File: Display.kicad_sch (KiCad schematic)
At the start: 9 parts, among them J2 TFT_LCD, U3 MT9284

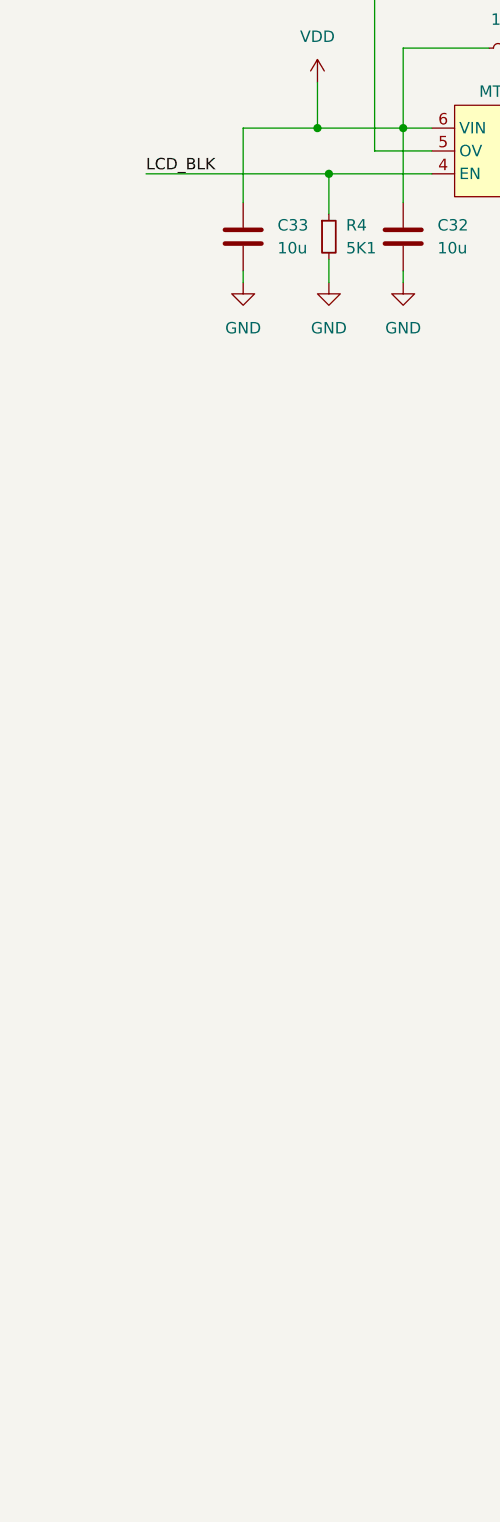
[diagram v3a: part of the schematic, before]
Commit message: Looks like FPC should be changed to XF2M-4015-1A
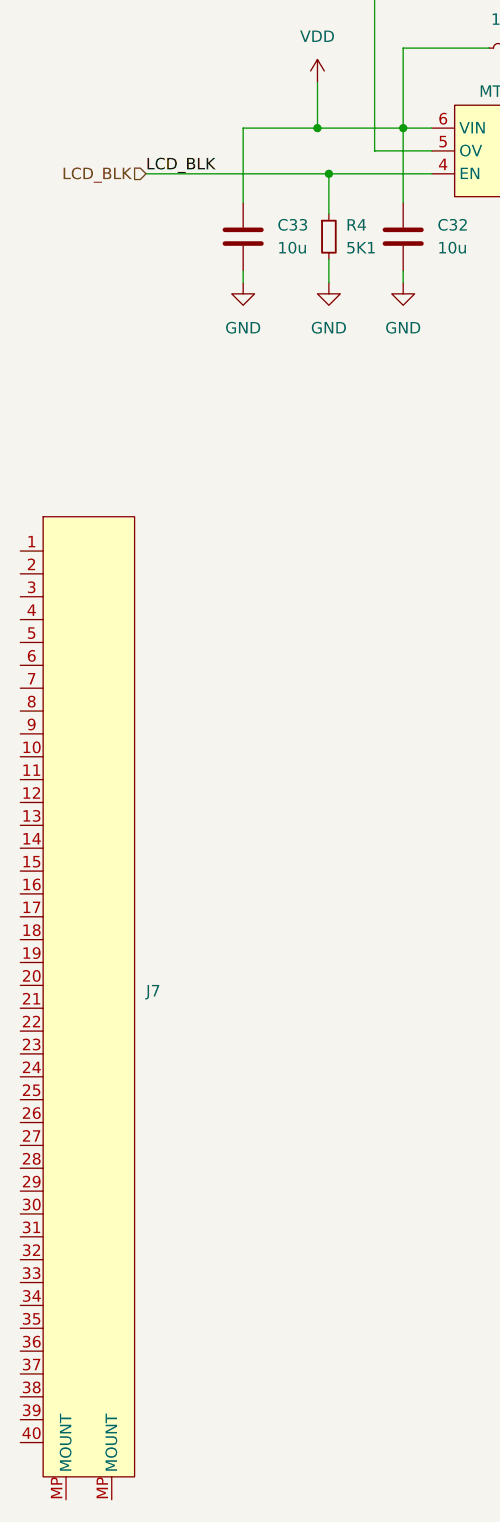
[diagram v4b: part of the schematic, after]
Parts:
- added J7: ~, FPC-40P-Omron-XF2M-4015-1Apretty:Omron-XF2M-4015-1A-R100-0-0-0, symbol FPC_40P_double_contact:FPC-40P
- D1: JLCPCB Part # (none) -> C345958
- J2: JLCPCB Part # (none) -> C225713
- R4: JLCPCB Part # (none) -> C25905
- U3: JLCPCB Part # (none) -> C181780
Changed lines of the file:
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@@
+		)
+	)
+	(hierarchical_label "LCD_BLK"
+		(shape input)
+		(at 57.15 48.26 180)
+		(fields_autoplaced yes)
+		(effects
+			(font
+				(size 1.27 1.27)
+			)
+			(justify right)
 		)
 	)
@@
 			)
 		)
+		(property "JLCPCB Part #" "C25905"
+			(at 77.47 55.245 0)
+			(effects
+				(font
+					(size 1.27 1.27)
+				)
+				(hide yes)
+			)
+		)
 		(pin "1"
 		)
@@
 			)
 		)
+		(property "JLCPCB Part #" ""
+			(at 97.79 34.29 0)
+			(effects
+				(font
+					(size 1.27 1.27)
+				)
+				(hide yes)
+			)
+		)
 		(pin "1"
 		)
@@
 			)
 		)
+		(property "JLCPCB Part #" ""
+			(at 67.945 55.245 0)
+			(effects
+				(font
+					(size 1.27 1.27)
+				)
+				(hide yes)
+			)
+		)
 		(pin "1"
 		)
@@
 			)
 		)
+		(property "JLCPCB Part #" ""
+			(at 113.03 53.34 0)
+			(effects
+				(font
+					(size 1.27 1.27)
+				)
+				(hide yes)
+			)
+		)
 		(pin "1"
 		)
@@
 			)
 		)
+		(property "JLCPCB Part #" ""
+			(at 85.725 55.245 0)
+			(effects
+				(font
+					(size 1.27 1.27)
+				)
+				(hide yes)
+			)
+		)
 		(pin "1"
 		)
@@
 		)
 		(property "Description" ""
+			(at 123.19 53.34 0)
+			(effects
+				(font
+					(size 1.27 1.27)
+				)
+				(hide yes)
+			)
+		)
+		(property "JLCPCB Part #" ""
 			(at 123.19 53.34 0)
 			(effects
@@
 			)
 		)
+		(property "JLCPCB Part #" "C345958"
+			(at 116.84 43.18 0)
+			(effects
+				(font
+					(size 1.27 1.27)
+				)
+				(hide yes)
+			)
+		)
 		(pin "1"
 		)
@@
 			)
 		)
+		(property "JLCPCB Part #" "C225713"
+			(at 209.55 133.35 0)
+			(effects
+				(font
+					(size 1.27 1.27)
+				)
+				(hide yes)
+			)
+		)
 		(pin "1"
 		)
@@
 			)
 		)
+		(property "JLCPCB Part #" "C181780"
+			(at 104.14 40.64 0)
+			(effects
+				(font
+					(size 1.27 1.27)
+				)
+				(hide yes)
+			)
+		)
 		(pin "1"
 		)
@@
 					(unit 1)
 				)
+			)
+		)
+	)
+	(symbol
+		(lib_name "FPC-40P_1")
+		(lib_id "FPC_40P_double_contact:FPC-40P")
+		(at 45.72 86.36 0)
+		(unit 1)
+		(exclude_from_sim no)
+		(in_bom yes)
+		(on_board yes)
+		(dnp no)
+		(fields_autoplaced yes)
+		(property "Reference" "J7"
+			(at 57.15 139.0649 0)
+			(effects
+				(font
+					(size 1.27 1.27)
+				)
+				(justify left)
+			)
+		)
+		(property "Value" "~"
+			(at 57.15 140.97 0)
+			(effects
+				(font
+					(size 1.27 1.27)
+				)
+				(justify left)
+			)
+		)
+		(property "Footprint" "FPC-40P-Omron-XF2M-4015-1Apretty:Omron-XF2M-4015-1A-R100-0-0-0"
+			(at 45.72 86.36 0)
+			(effects
+				(font
+					(size 1.27 1.27)
+				)
+				(hide yes)
+			)
+		)
+		(property "Datasheet" ""
+			(at 45.72 86.36 0)
+			(effects
+				(font
+					(size 1.27 1.27)
+				)
+				(hide yes)
+			)
+		)
+		(property "Description" ""
+			(at 45.72 86.36 0)
+			(effects
+				(font
+					(size 1.27 1.27)
+				)
+				(hide yes)
+			)
+		)
+		(pin "33"
+		)
+		(pin "17"
+		)
+		(pin "30"
+		)
+		(pin "32"
+		)
+		(pin "38"
+		)
+		(pin "2"
+		)
+		(pin "40"
+		)
+		(pin "34"
+		)
+		(pin "31"
+		)
+		(pin "27"
+		)
+		(pin "5"
+		)
+		(pin "4"
+		)
+		(pin "22"
+		)
+		(pin "6"
+		)
+		(pin "25"
+		)
+		(pin "9"
+		)
+		(pin "20"
+		)
+		(pin "36"
+		)
+		(pin "37"
+		)
+		(pin "12"
+		)
+		(pin "11"
+		)
+		(pin "10"
+		)
+		(pin "1"
+		)
+		(pin "8"
+		)
+		(pin "13"
+		)
+		(pin "MP"
+		)
+		(pin "14"
+		)
+		(pin "16"
+		)
+		(pin "21"
+		)
+		(pin "26"
+		)
+		(pin "19"
+		)
+		(pin "15"
+		)
+		(pin "39"
+		)
+		(pin "29"
+		)
+		(pin "35"
+		)
+		(pin "23"
+		)
+		(pin "24"
+		)
+		(pin "3"
+		)
+		(pin "7"
+		)
+		(pin "28"
+		)
+		(pin "18"
+		)
+		(pin "MP"
+		)
+		(instances
+			(project "H743_LCD_dev"
+				(path "/70094798-b7e4-48a4-a512-b8f48be18f9f/99abf84f-89dd-4209-b43f-cdbcbe391aaa"
+					(reference "J7")
+					(unit 1)
+				)

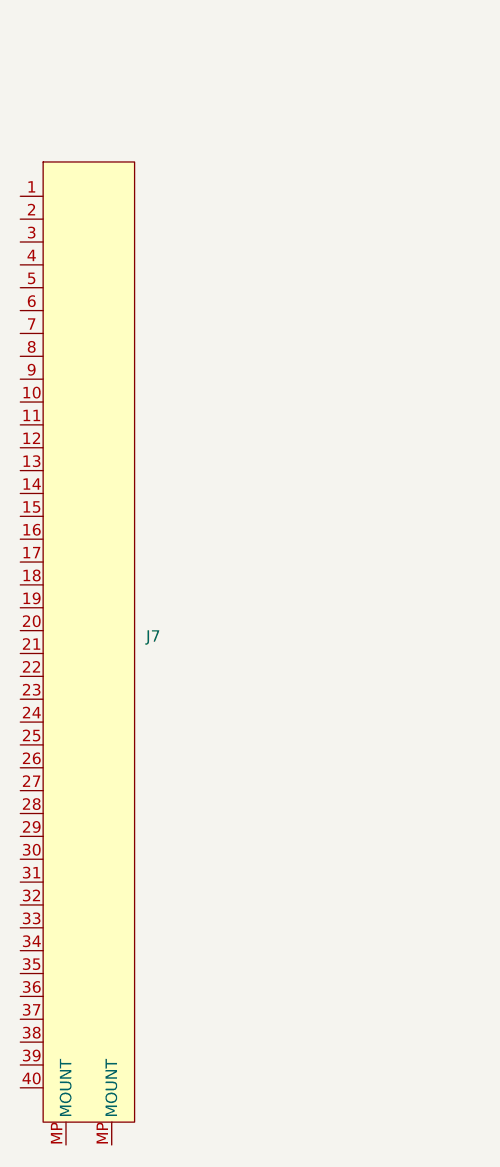
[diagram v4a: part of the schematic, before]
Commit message: Changed the FPC footprint and uart, added RTC battery connector
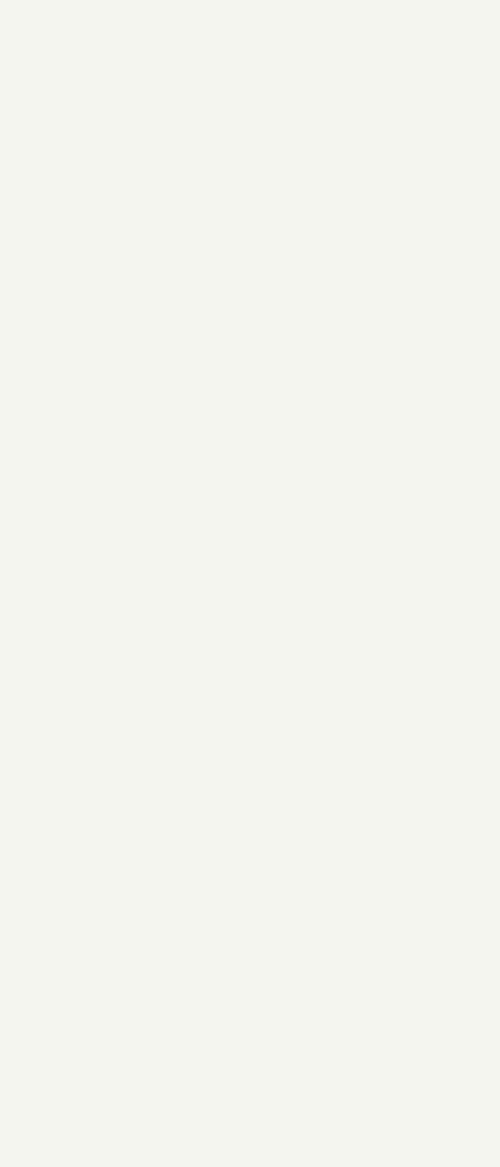
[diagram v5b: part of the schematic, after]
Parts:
- removed J7: ~, FPC-40P-Omron-XF2M-4015-1Apretty:Omron-XF2M-4015-1A-R100-0-0-0, symbol FPC_40P_double_contact:FPC-40P
- J2: footprint Connector_FFC-FPC:Hirose_FH12-40S-0.5SH_1x40-1MP_P0.50mm_Horizontal -> FPC-40P-Omron-XF2M-4015-1Apretty:Omron-XF2M-4015-1A-R100-0-0-0
- R3: JLCPCB Part # (none) -> C166483

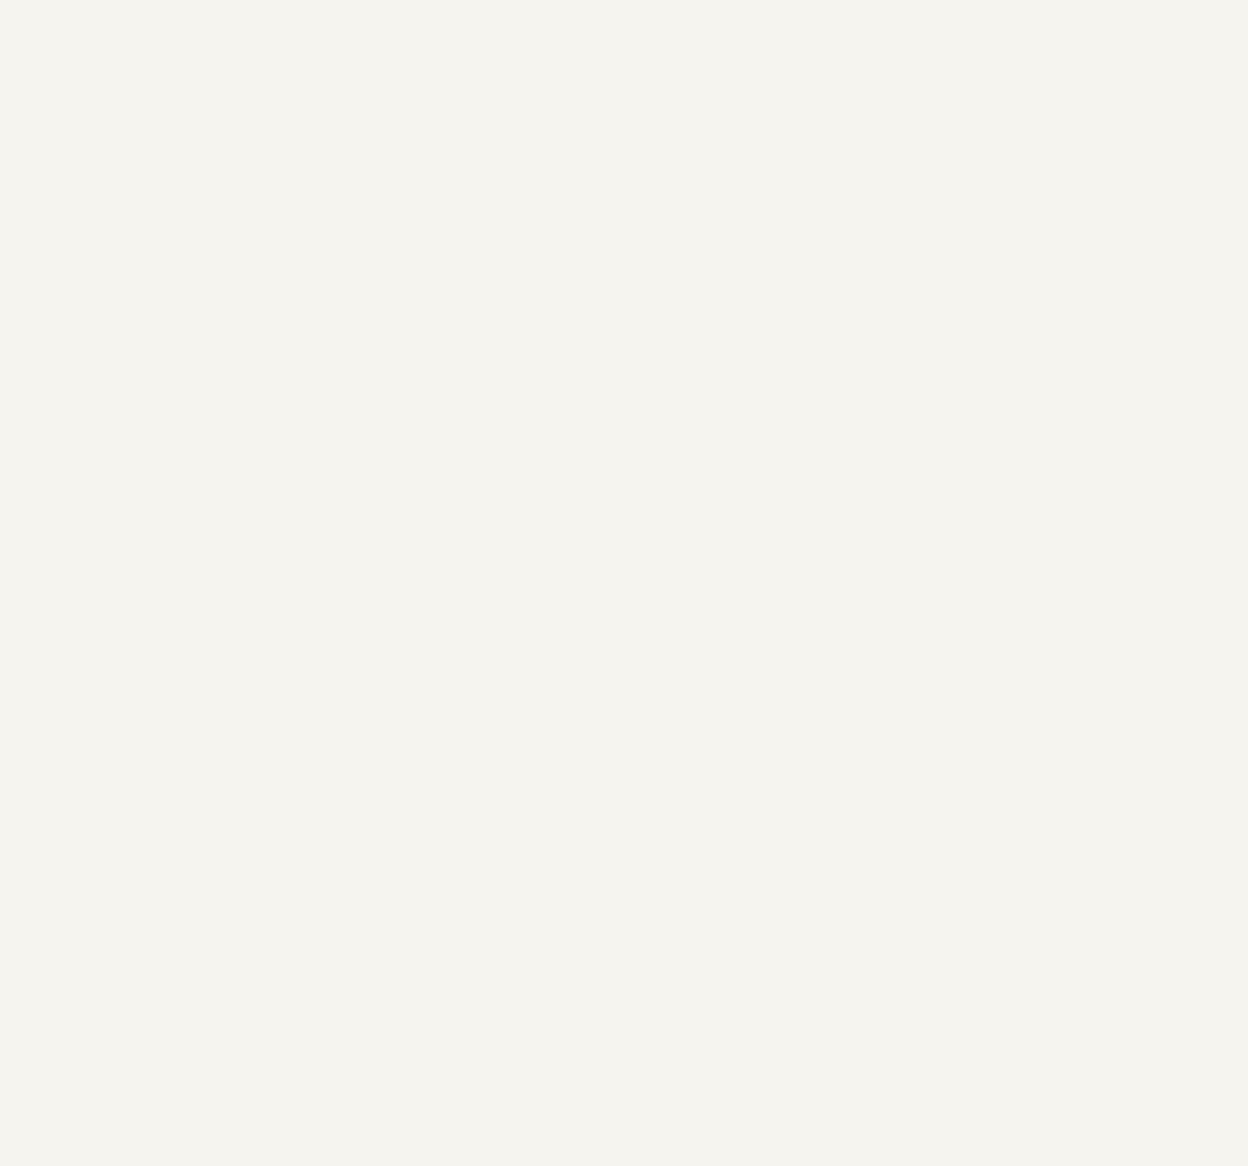
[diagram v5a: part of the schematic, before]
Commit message: Added UART esd
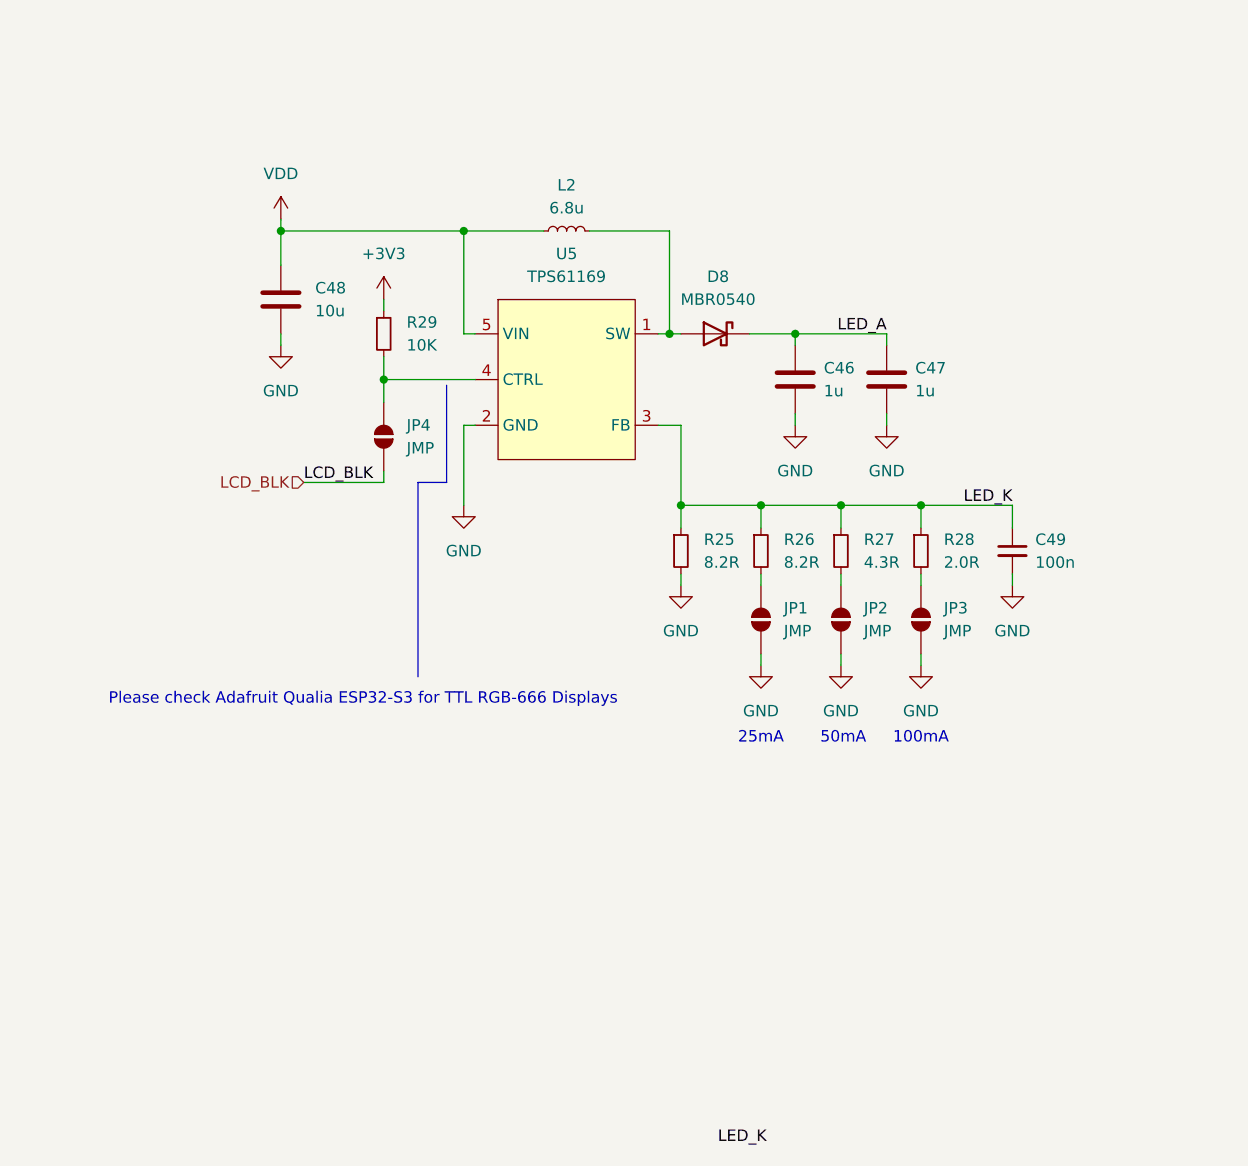
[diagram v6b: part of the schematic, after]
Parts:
- added C46, C47: 1u, Capacitor_SMD:C_0603_1608Metric, symbol Device:C
- added C48: 10u, Capacitor_SMD:C_0603_1608Metric, symbol Device:C
- added C49: 100n, Capacitor_SMD:C_0402_1005Metric, symbol Device:C_Small
- added D8: MBR0540, Diode_SMD:D_SOD-123, symbol Diode:MBR0540
- added JP1, JP2, JP3, JP4: JMP, Jumper:SolderJumper-2_P1.3mm_Open_RoundedPad1.0x1.5mm, symbol Jumper:SolderJumper_2_Open
- added L2: 6.8u, Inductor_SMD:L_1210_3225Metric, symbol Device:L_Small
- added R25, R26: 8.2R, Resistor_SMD:R_0402_1005Metric, symbol Device:R_Small
- added R27: 4.3R, Resistor_SMD:R_0402_1005Metric, symbol Device:R_Small
- added R28: 2.0R, Resistor_SMD:R_0402_1005Metric, symbol Device:R_Small
- added R29: 10K, Resistor_SMD:R_0402_1005Metric, symbol Device:R_Small
- added U5: TPS61169, Package_TO_SOT_SMD:SOT-353_SC-70-5, symbol TPS61169:TPS61169
- C31: JLCPCB Part # (none) -> C15849
- C32, C33: JLCPCB Part # (none) -> C96446
- L1: JLCPCB Part # (none) -> C189932
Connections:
- net +3V3: now also R29.1
- net GND: now also C46.2, C47.2, C48.2, C49.2, JP1.1 (A), JP2.1 (A), JP3.1 (A), R25.2, U5.2 (GND)
- net LCD_BLK: now also JP4.1 (A)
- net LED_A: now also C46.1, C47.1, D8.1 (K)
- net LED_K: now also C49.1, R25.1, R26.1, R27.1, R28.1, U5.3 (FB)
- net VDD: now also C48.1, L2.1, U5.5 (VIN)
- new net: JP1.2 (B), R26.2
- new net: JP2.2 (B), R27.2
- new net: JP3.2 (B), R28.2
- new net: JP4.2 (B), R29.2, U5.4 (CTRL)
- new net: D8.2 (A), L2.2, U5.1 (SW)
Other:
- note added: "100mA"
- note added: "25mA"
- note added: "50mA"
- note added: "Please check Adafruit Qualia ESP32-S3 for TTL RGB-666 Displays"

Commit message: All clear (need verification), need add capacitor next to I2C conn, verify I2S gain
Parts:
- C31, C32, C33, D1, L1, R3, R4, U3: now not fitted; now left out of the parts list
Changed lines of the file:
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@@
 		)
 	)
+	(hierarchical_label "LCD_BLK"
+		(shape input)
+		(at 43.18 130.81 180)
+		(fields_autoplaced yes)
+		(effects
+			(font
+				(size 1.27 1.27)
+			)
+			(justify right)
+		)
+	)
 	(hierarchical_label "LCD_TP_SDA"
 		(shape bidirectional)
@@
 		)
 	)
-	(hierarchical_label "LCD_BLK"
-		(shape input)
-		(at 43.18 130.81 180)
-		(fields_autoplaced yes)
-		(effects
-			(font
-				(size 1.27 1.27)
-			)
-			(justify right)
-		)
-	)
 	(hierarchical_label "LCD_RESET"
 		(shape input)
@@
 		(unit 1)
 		(exclude_from_sim no)
-		(in_bom yes)
-		(on_board yes)
-		(dnp no)
+		(in_bom no)
+		(on_board no)
+		(dnp yes)
 		(fields_autoplaced yes)
 		(property "Reference" "R4"
@@
 		(unit 1)
 		(exclude_from_sim no)
-		(in_bom yes)
-		(on_board yes)
-		(dnp no)
+		(in_bom no)
+		(on_board no)
+		(dnp yes)
 		(fields_autoplaced yes)
 		(property "Reference" "L1"
@@
 		(unit 1)
 		(exclude_from_sim no)
-		(in_bom yes)
-		(on_board yes)
-		(dnp no)
+		(in_bom no)
+		(on_board no)
+		(dnp yes)
 		(fields_autoplaced yes)
 		(property "Reference" "C33"
@@
 		(unit 1)
 		(exclude_from_sim no)
-		(in_bom yes)
-		(on_board yes)
-		(dnp no)
+		(in_bom no)
+		(on_board no)
+		(dnp yes)
 		(fields_autoplaced yes)
 		(property "Reference" "R3"
@@
 		(unit 1)
 		(exclude_from_sim no)
-		(in_bom yes)
-		(on_board yes)
-		(dnp no)
+		(in_bom no)
+		(on_board no)
+		(dnp yes)
 		(fields_autoplaced yes)
 		(property "Reference" "C32"
@@
 		(unit 1)
 		(exclude_from_sim no)
-		(in_bom yes)
-		(on_board yes)
-		(dnp no)
+		(in_bom no)
+		(on_board no)
+		(dnp yes)
 		(fields_autoplaced yes)
 		(property "Reference" "C31"
@@
 		(unit 1)
 		(exclude_from_sim no)
-		(in_bom yes)
-		(on_board yes)
-		(dnp no)
+		(in_bom no)
+		(on_board no)
+		(dnp yes)
 		(fields_autoplaced yes)
 		(property "Reference" "D1"
@@
 		(unit 1)
 		(exclude_from_sim no)
-		(in_bom yes)
-		(on_board yes)
-		(dnp no)
+		(in_bom no)
+		(on_board no)
+		(dnp yes)
 		(property "Reference" "U3"
 			(at 97.663 37.084 0)

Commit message: Finished. 1st version, ordered 1st batch
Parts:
- L2: footprint Inductor_SMD:L_1210_3225Metric -> Inductor_SMD:L_Changjiang_FNR5012S; JLCPCB Part # C844992 -> C2847472
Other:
- note added: "Verified"
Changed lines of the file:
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@@
 		)
 	)
+	(text "Verified"
+		(exclude_from_sim no)
+		(at 224.536 83.82 0)
+		(effects
+			(font
+				(size 1.27 1.27)
+			)
+		)
+	)
 	(text "Please check Adafruit Qualia ESP32-S3 for TTL RGB-666 Displays"
 		(exclude_from_sim no)
@@
 			)
 		)
-		(property "Footprint" "Inductor_SMD:L_1210_3225Metric"
+		(property "Footprint" "Inductor_SMD:L_Changjiang_FNR5012S"
 			(at 72.39 102.87 0)
 			(effects
@@
 			)
 		)
-		(property "JLCPCB Part #" "C844992"
+		(property "JLCPCB Part #" "C2847472"
 			(at 72.39 102.87 0)
 			(effects
